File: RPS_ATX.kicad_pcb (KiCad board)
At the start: 2 copper layers, 100 x 50 mm, 93 parts, among them J10 DISP, J11 ENC1, J12 ENC2, J2 C1, J3 C2, J4 17.5V, J5 PS_OUT-, J6 PS_OUT+, J7 RPS_OUT+, J8 SWD, J9 RPS_OUT-, Q1 AO3400A, Q3 BSS138, U1 TL494, U2 AMS1117-3.3, U3 L7815, U5 INA180A2, U6 ICL7660, U7 LM7805_TO220, U8 STM32G431RBT6, U9 OP07, Y1 8MHz

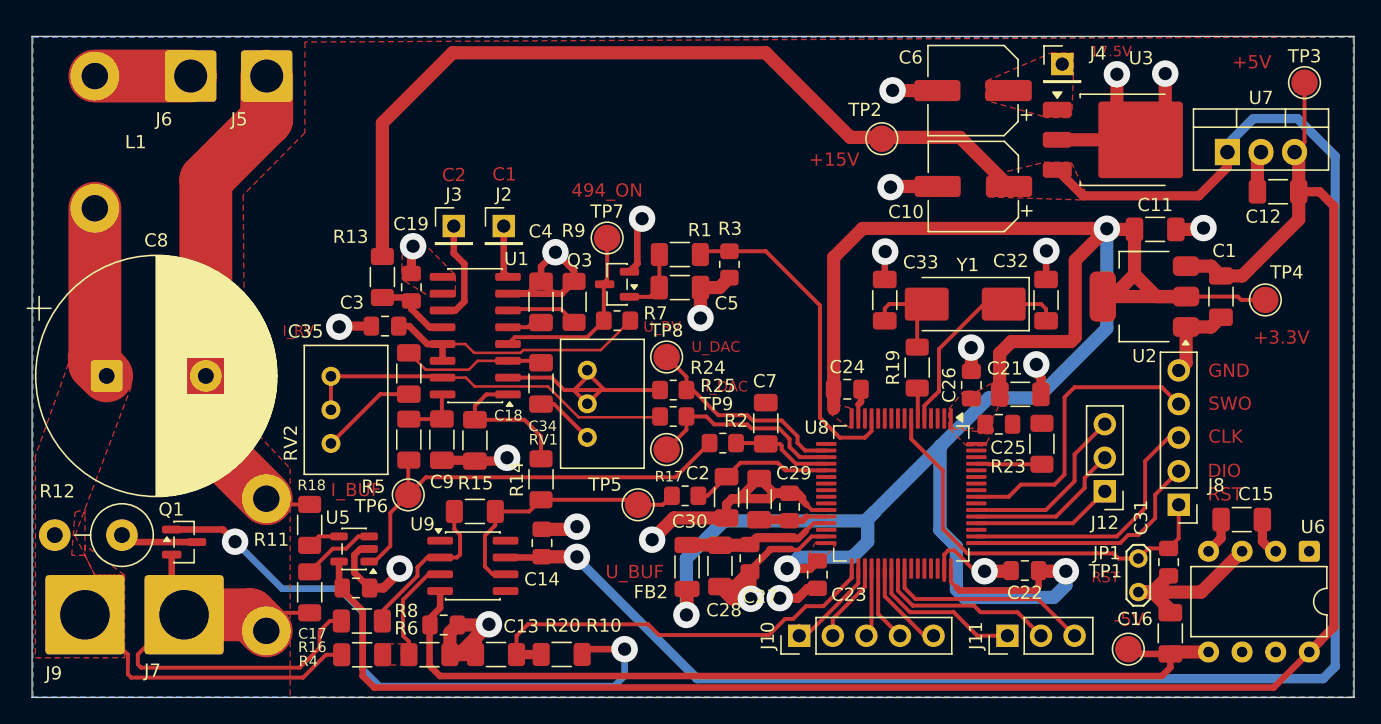
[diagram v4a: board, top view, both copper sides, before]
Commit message: added fan control and ds18b20 to the schematic
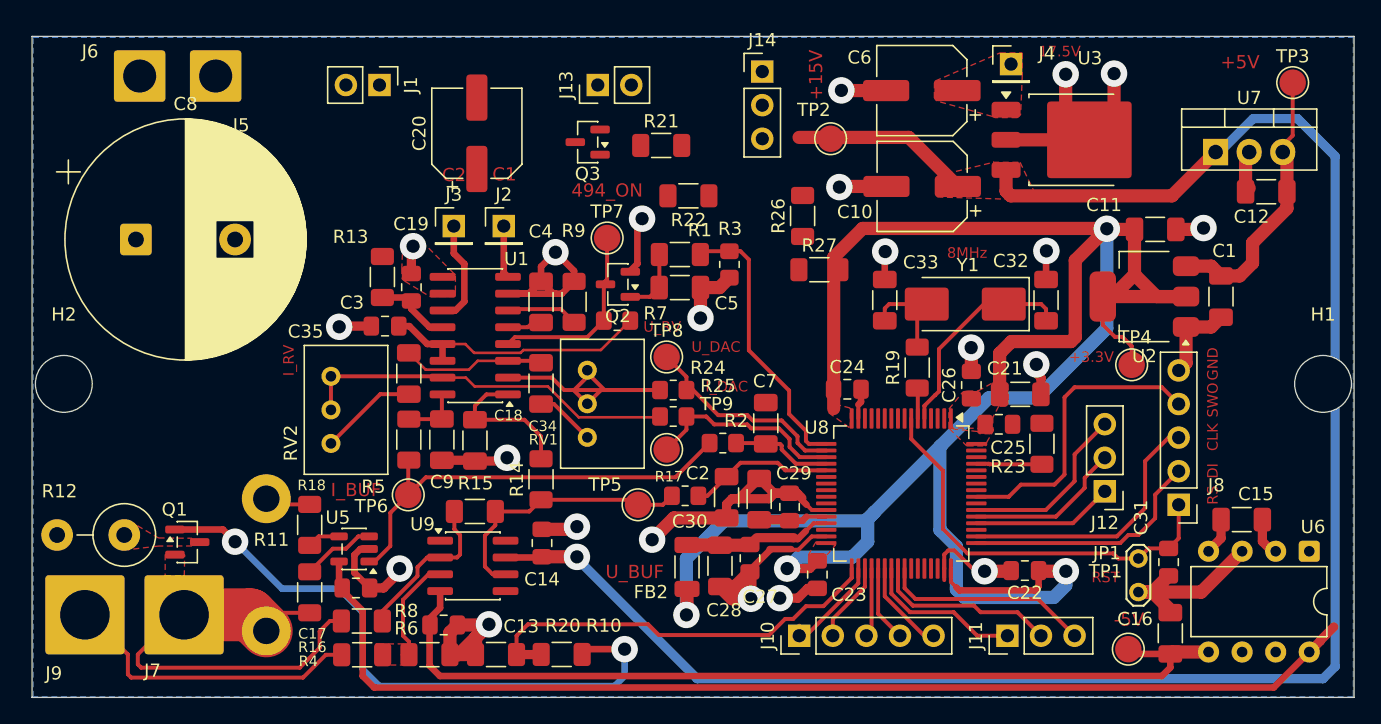
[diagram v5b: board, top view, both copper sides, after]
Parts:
- removed L1: L, my lib:Resistor_Shunt_L10_D3.7
- added C20: 100uF, Capacitor_SMD:CP_Elec_6.3x5.4_Nichicon, F.Cu at (88.6, 62.6)
- added H1: MountingHole, MountingHole:MountingHole_4.3mm_M4, F.Cu at (152.7, 81.5)
- added H2: MountingHole, MountingHole:MountingHole_4.3mm_M4, F.Cu at (57.4, 81.5)
- added J1: Fan_in, Connector_PinHeader_2.54mm:PinHeader_1x02_P2.54mm_Vertical, F.Cu at (81.3, 58.9)
- added J13: Fan_out, Connector_PinHeader_2.54mm:PinHeader_1x02_P2.54mm_Vertical, F.Cu at (97.8, 58.9)
- added J14: TEMP_SEN, Connector_PinHeader_2.54mm:PinHeader_1x03_P2.54mm_Vertical, F.Cu at (110.2, 57.9)
- added Q2: AO3400A, Package_TO_SOT_SMD:SOT-23, F.Cu at (99.3, 74.0)
- added R21: 5.1K, Resistor_SMD:R_1206_3216Metric_Pad1.30x1.75mm_HandSolder, F.Cu at (102.6, 63.5)
- added R22: 100R, Resistor_SMD:R_1206_3216Metric_Pad1.30x1.75mm_HandSolder, F.Cu at (104.6, 67.3)
- added R26: 470R, Resistor_SMD:R_1206_3216Metric_Pad1.30x1.75mm_HandSolder, F.Cu at (113.3, 68.8)
- added R27: 470R, Resistor_SMD:R_1206_3216Metric_Pad1.30x1.75mm_HandSolder, F.Cu at (114.6, 72.9)
- Q3: value BSS138 -> AO3400A
- moved TP4 11.2 mm to (138.2, 80.1)
- moved Q3 11.0 mm to (97.0, 63.2)
- moved C8 10.6 mm to (62.9, 70.6)
- moved J4 3.87 mm to (129.1, 57.3)
- moved C10 3.87 mm to (122.3, 66.6)
- moved TP2 3.87 mm to (115.4, 63.0)
- moved C6 3.87 mm to (122.3, 59.3)
- moved U3 3.87 mm to (133.7, 63.1)
- moved J5 3.86 mm to (68.9, 58.2)
- moved J6 3.86 mm to (63.1, 58.2)
- moved C12 0.89 mm to (148.4, 67.0)
- moved TP3 0.89 mm to (150.4, 58.8)
- moved U7 0.89 mm to (144.5, 64.0)
- moved Q1 0.24 mm to (66.7, 93.5)
- moved R12 0.18 mm to (62.0, 93.0)
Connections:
- C5 pad 1: Net-(Q3-G) -> Net-(Q2-G)
- J6 pad 1: Net-(J6-Pin_1) -> VOUT
- Q3 pad 2: GND -> Net-(J13-Pin_2)
- Q3 pad 3: DTC -> Net-(J1-Pin_1)
- R1 pad 2: Net-(Q3-G) -> Net-(Q2-G)
- U8 pad 13: MCU_494_ON -> unconnected-(U8-PA1-Pad13)
- U8 pad 17: unconnected-(U8-PA3-Pad17) -> MCU_494_ON
- U8 pad 22: unconnected-(U8-PC4-Pad22) -> MCU_TEMP
- U8 pad 24: unconnected-(U8-PB0-Pad24) -> MCU_FAN
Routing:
- net +15V: track 196.0 -> 149.4 mm
- net +5V: track 141.9 -> 106.0 mm
- net GND: track 205.2 -> 171.7 mm
- net VOUT: track 36.0 -> 23.0 mm
- net Net-(J6-Pin_1): track 7.25 -> 0.00 mm
- net Net-(Q1-D): track 6.44 -> 0.00 mm
- net Net-(Q3-G): track 5.05 -> 0.00 mm
- net Net-(Q2-G): track 0.00 -> 5.05 mm
- net MCU_494_ON: track 25.0 -> 21.2 mm
- net MEAS_I+: track 40.5 -> 36.9 mm
- added copper zone on F.Cu, net MEAS_I+
- added copper zone on F.Cu, net Net-(Q1-D)
- removed copper zone on F.Cu, net VOUT
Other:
- board text added: "DI"
- board text added: "RS"
- board text removed: "DIO"
- board text removed: "RST"

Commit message: fan and temp sensor tracing
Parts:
- added C36: 10u, Capacitor_SMD:C_1206_3216Metric_Pad1.33x1.80mm_HandSolder, F.Cu at (151.6, 91.8)
- J1, J13: footprint Connector_PinHeader_2.54mm:PinHeader_1x02_P2.54mm_Vertical -> Connector_JST:JST_XH_B2B-XH-A_1x02_P2.50mm_Vertical
- J14: footprint Connector_PinHeader_2.54mm:PinHeader_1x03_P2.54mm_Vertical -> Connector_JST:JST_XH_B3B-XH-A_1x03_P2.50mm_Vertical
- moved R22 13.7 mm to (91.4, 63.5), turned to 90 degrees
- moved R21 9.18 mm to (94.2, 67.3), turned to 90 degrees
- moved Q3 6.01 mm to (92.5, 59.2)
- moved C20 2.30 mm to (86.4, 62.3)
- moved J13 2.30 mm to (98.0, 61.2)
- moved R26 2.05 mm to (111.3, 69.1)
- moved J1 1.86 mm to (79.5, 59.5)
- moved J14 1.86 mm to (110.7, 59.7), turned to 180 degrees
- moved TP2 1.69 mm to (117.1, 63.0)
- moved C12 0.31 mm to (148.6, 66.8)
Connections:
- net Net-(J1-Pin_2) renamed /fan+
- net Net-(J13-Pin_2) renamed /fan-
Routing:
- net +15V: track 149.4 -> 212.6 mm
- net MCU_FAN: track 0.00 -> 51.3 mm
- net VOUT: track 23.0 -> 69.8 mm
- net +5V: track 106.0 -> 145.7 mm
- net GND: track 171.7 -> 211.0 mm, vias 22 -> 24
- net MCU_TEMP: track 0.00 -> 24.3 mm
- net /fan+: track 0.00 -> 22.6 mm
- net +3.3V: track 175.7 -> 189.2 mm
- net Net-(J1-Pin_1): track 0.00 -> 12.3 mm
- net Net-(J14-Pin_2): track 0.00 -> 9.09 mm
- net /fan-: track 0.00 -> 4.74 mm
- net Net-(Q3-G): track 0.00 -> 3.35 mm
- net Net-(U1-RT): track 5.46 -> 6.52 mm
- net DTC: track 14.3 -> 15.1 mm
- net +5V_REF: track 20.6 -> 21.2 mm
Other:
- board text added: "+"
- board text added: "IN+"

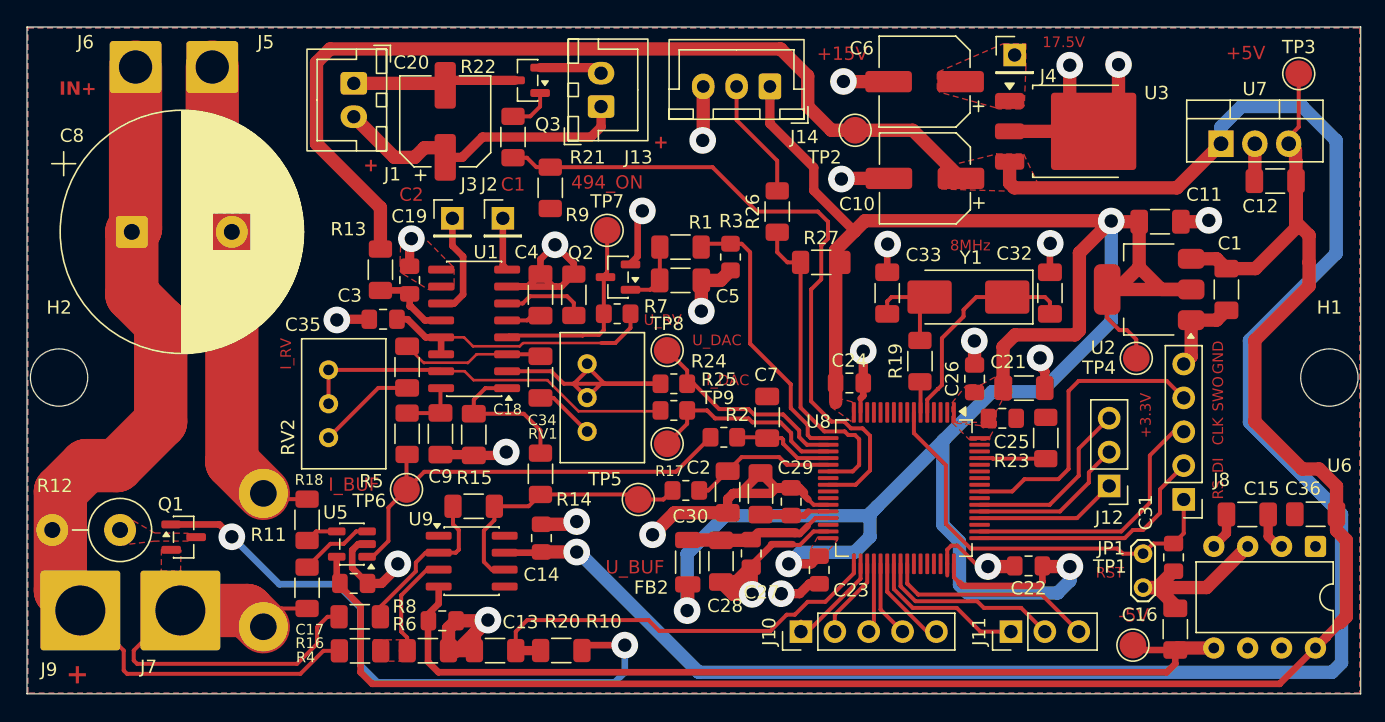
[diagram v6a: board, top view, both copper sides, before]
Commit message: minor changes (0805 for 0.1% R, new Y)
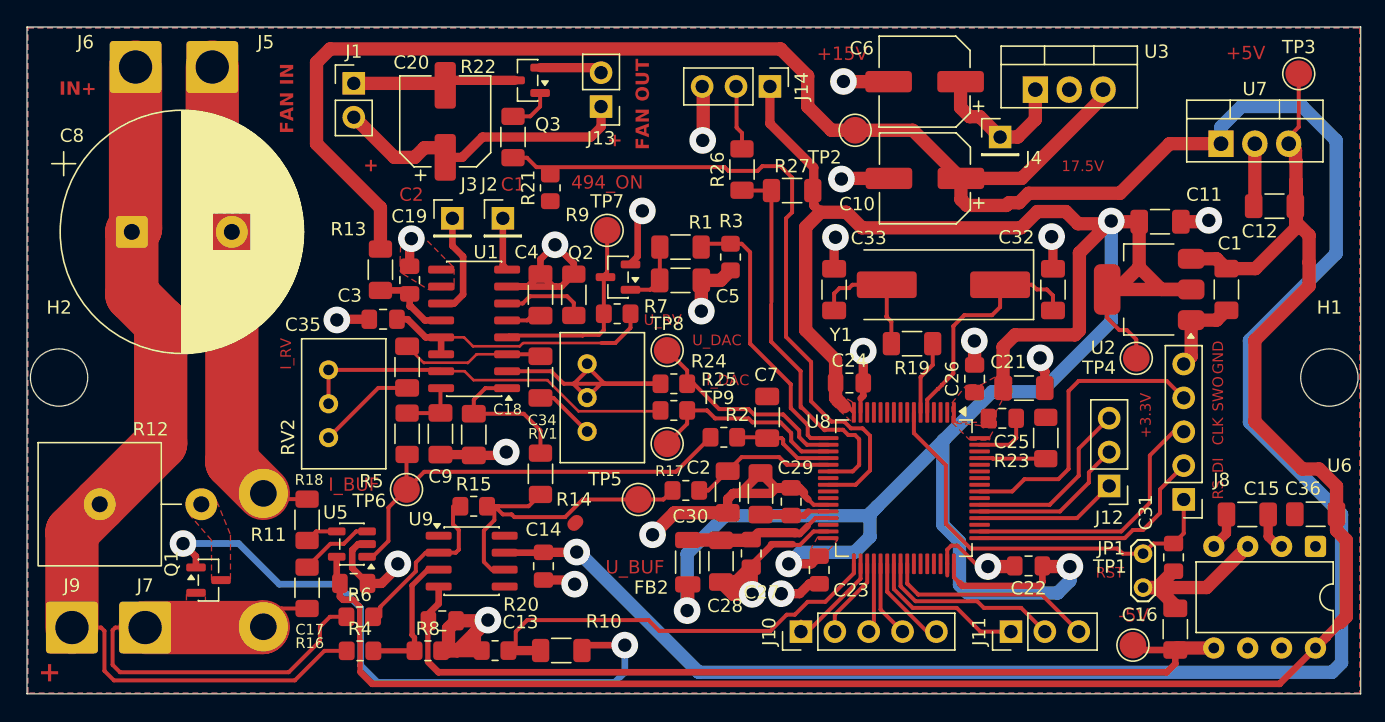
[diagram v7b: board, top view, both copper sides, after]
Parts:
- C18, C9: value 10n -> 1n
- J1, J13: footprint Connector_JST:JST_XH_B2B-XH-A_1x02_P2.50mm_Vertical -> Connector_PinHeader_2.54mm:PinHeader_1x02_P2.54mm_Vertical
- J14: footprint Connector_JST:JST_XH_B3B-XH-A_1x03_P2.50mm_Vertical -> Connector_PinHeader_2.54mm:PinHeader_1x03_P2.54mm_Vertical
- J7, J9: footprint Connector_Wire:SolderWire-4sqmm_1x01_D3mm_OD6mm -> Connector_Wire:SolderWire-2sqmm_1x01_D2mm_OD3.9mm
- R12: footprint Resistor_THT:R_Axial_DIN0414_L11.9mm_D4.5mm_P5.08mm_Vertical -> Resistor_THT:R_Axial_Power_L25.0mm_W9.0mm_P7.62mm_Vertical
- R14, R5: value 1.5K -> 15K
- R15, R20, R21, R4, R6, R8: footprint Resistor_SMD:R_1206_3216Metric_Pad1.30x1.75mm_HandSolder -> Resistor_SMD:R_0805_2012Metric_Pad1.20x1.40mm_HandSolder
- U3: footprint Package_TO_SOT_SMD:TO-252-3_TabPin2 -> Package_TO_SOT_THT:TO-220-3_Vertical
- U6: value ICL7660 -> ICL7660A
- Y1: footprint Crystal:Crystal_SMD_0603-2Pin_6.0x3.5mm_HandSoldering -> Crystal:Crystal_SMD_HC49-SD
- moved J4 6.25 mm to (128.0, 63.5)
- moved R27 5.81 mm to (112.4, 67.5)
- moved U3 4.41 mm to (130.6, 59.9)
- moved R26 4.11 mm to (108.6, 65.9)
- moved C33 3.99 mm to (115.5, 74.9)
- moved Q1 3.72 mm to (68.6, 96.7)
- moved J7 2.94 mm to (63.9, 100.3)
- moved R12 2.46 mm to (60.5, 91.0), turned to 0 degrees
- moved C14 2.11 mm to (93.7, 95.7), turned to -90 degrees
- moved Y1 2.09 mm to (123.7, 74.6)
- moved C12 1.88 mm to (148.5, 68.7)
- moved R19 1.44 mm to (121.4, 79.0), turned to 180 degrees
- moved J9 1.43 mm to (58.4, 100.3)
- moved C32 0.34 mm to (131.9, 74.9)
- turned J1 to 0 degrees
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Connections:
- R12 pad 1: Net-(Q1-D) -> VOUT
- R12 pad 2: VOUT -> Net-(Q1-D)
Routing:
- net +15V: track 212.6 -> 230.6 mm
- net +17.5V_ATX: track 0.00 -> 11.3 mm
- net GND: track 211.0 -> 200.3 mm, vias 24 -> 22
- net +3.3V: track 189.2 -> 194.8 mm
- net Net-(R14-Pad1): track 20.5 -> 25.5 mm
- net MCU_TEMP: track 24.3 -> 29.1 mm
- net Net-(J14-Pin_2): track 9.09 -> 4.85 mm
- net MCU_OSC_OUT: track 2.32 -> 5.53 mm
- net Net-(U9-+): track 8.45 -> 11.4 mm
- net Net-(C33-Pad1): track 7.80 -> 10.1 mm
- net MCU_OSC_IN: track 16.8 -> 18.5 mm
- net Net-(Q1-D): track 0.00 -> 0.65 mm
- removed copper zone on F.Cu, net +15V
- removed copper zone on F.Cu, net +17.5V_ATX
- removed copper zone on F.Cu, net Net-(U9-+)
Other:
- board text added: "FAN IN"
- board text added: "FAN OUT"
